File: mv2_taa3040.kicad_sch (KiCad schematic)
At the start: 13 parts, among them U1 TAA3040

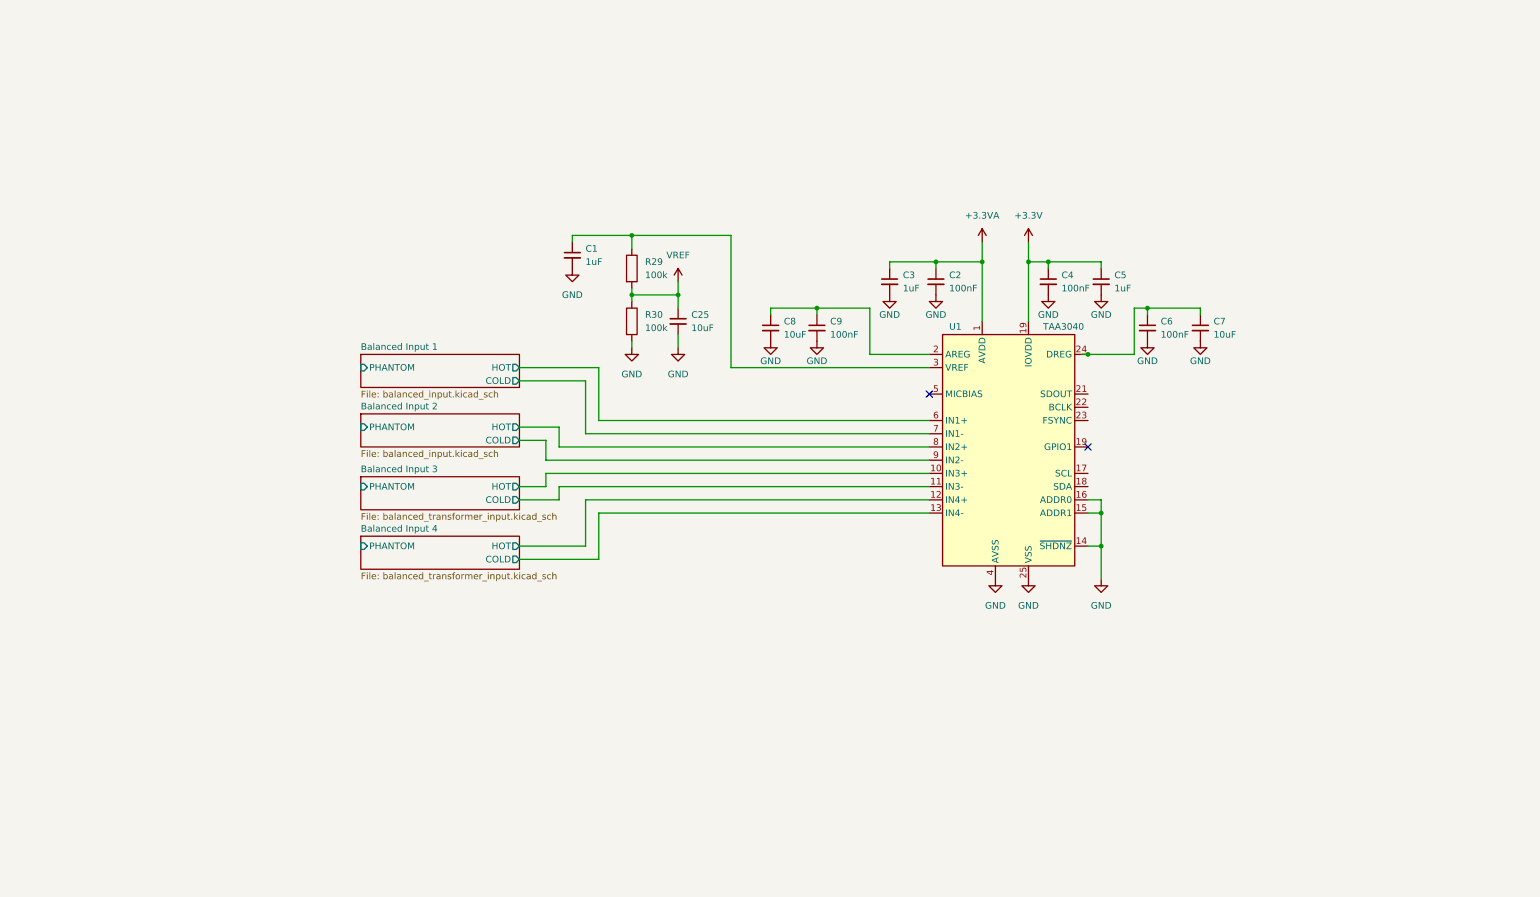
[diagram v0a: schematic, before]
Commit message: some suggested changes to the schematic:
- common pull-down mosfet for phantom power switch
- added board interconnect header
- proposed buffer for VREF
- cosmetic changes
- address selection jumpers
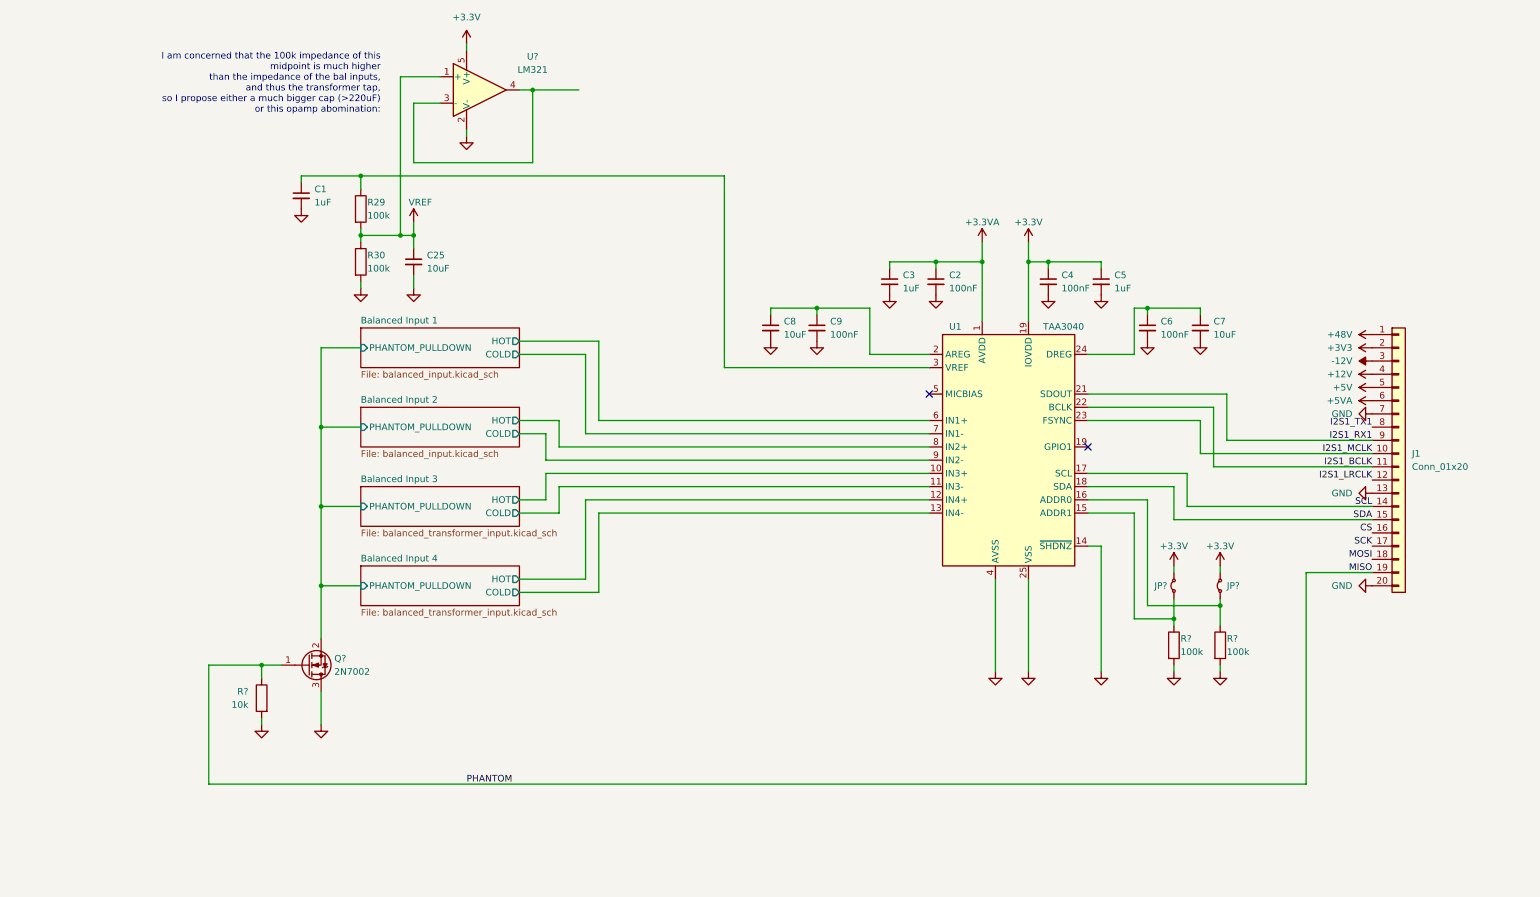
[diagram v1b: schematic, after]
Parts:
- added J1: Conn_01x20, Connector_PinHeader_2.54mm:PinHeader_1x20_P2.54mm_Vertical, symbol Connector_Generic:Conn_01x20
- added JP? (x2): Jumper_2_Small_Bridged, symbol Jumper:Jumper_2_Small_Bridged
- added Q?: 2N7002, Package_TO_SOT_SMD:SOT-23, symbol Transistor_FET:2N7002
- added R? (x2): 100k, Resistor_SMD:R_0603_1608Metric, symbol Device:R
- added R?: 10k, Resistor_SMD:R_0603_1608Metric, symbol Device:R
- added U?: LM321, Package_TO_SOT_SMD:SOT-23-5, symbol Amplifier_Operational:LM321
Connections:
- net +3.3V: now also JP?.2 (B), JP?.2 (B), U?.5 (V+)
- net GND: now also J1.13 (Pin_13), J1.20 (Pin_20), J1.7 (Pin_7), Q?.3 (D), R?.2, R?.2, R?.2, U?.2 (V-); no longer U1.15 (ADDR1), U1.16 (ADDR0)
- net VREF: now also U?.1 (+)
- net SCL: now reaches U1.17 (SCL)
- net SCL: now also J1.14 (Pin_14)
- net SDA: now reaches U1.18 (SDA)
- net SDA: now also J1.15 (Pin_15)
- net I2S1_RX1: now reaches U1.21 (SDOUT)
- net I2S1_RX1: now also J1.9 (Pin_9)
- net I2S1_BCLK: now reaches U1.22 (BCLK)
- net I2S1_BCLK: now also J1.11 (Pin_11)
- net I2S1_MCLK: now reaches U1.23 (FSYNC)
- net I2S1_MCLK: now also J1.10 (Pin_10)
- new net: U?.3 (-), U?.4
- new net: JP?.1 (A), R?.1, U1.16 (ADDR0)
- new net: JP?.1 (A), R?.1, U1.15 (ADDR1)
- new net +12V: J1.4 (Pin_4)
- new net +3V3: J1.2 (Pin_2)
- new net +48V: J1.1 (Pin_1)
- new net +5V: J1.5 (Pin_5)
- new net +5VA: J1.6 (Pin_6)
- new net -12V: J1.3 (Pin_3)
- new net Balanced Input 1/PHANTOM_PULLDOWN: Q?.2 (S)
- new net CS: J1.16 (Pin_16)
- new net I2S1_LRCLK: J1.12 (Pin_12)
- new net I2S1_TX1: J1.8 (Pin_8)
- new net MISO: J1.19 (Pin_19), Q?.1 (G), R?.1
- new net MOSI: J1.18 (Pin_18)
- new net SCK: J1.17 (Pin_17)
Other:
- sheet Balanced Input 1 ports: added PHANTOM_PULLDOWN; removed PHANTOM
- sheet Balanced Input 2 ports: added PHANTOM_PULLDOWN; removed PHANTOM
- sheet Balanced Input 3 ports: added PHANTOM_PULLDOWN; removed PHANTOM
- sheet Balanced Input 4 ports: added PHANTOM_PULLDOWN; removed PHANTOM
- note added: "I am concerned that the 100k impedance of this midpoint is much higher than the impedance of the bal inputs, and thus the transformer tap, so I propose either a much bigger cap (>220uF) or this opamp abomination:"
- moved on the sheet: C1, C25, R29, R30

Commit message: independent phantom control and removed transformer bias
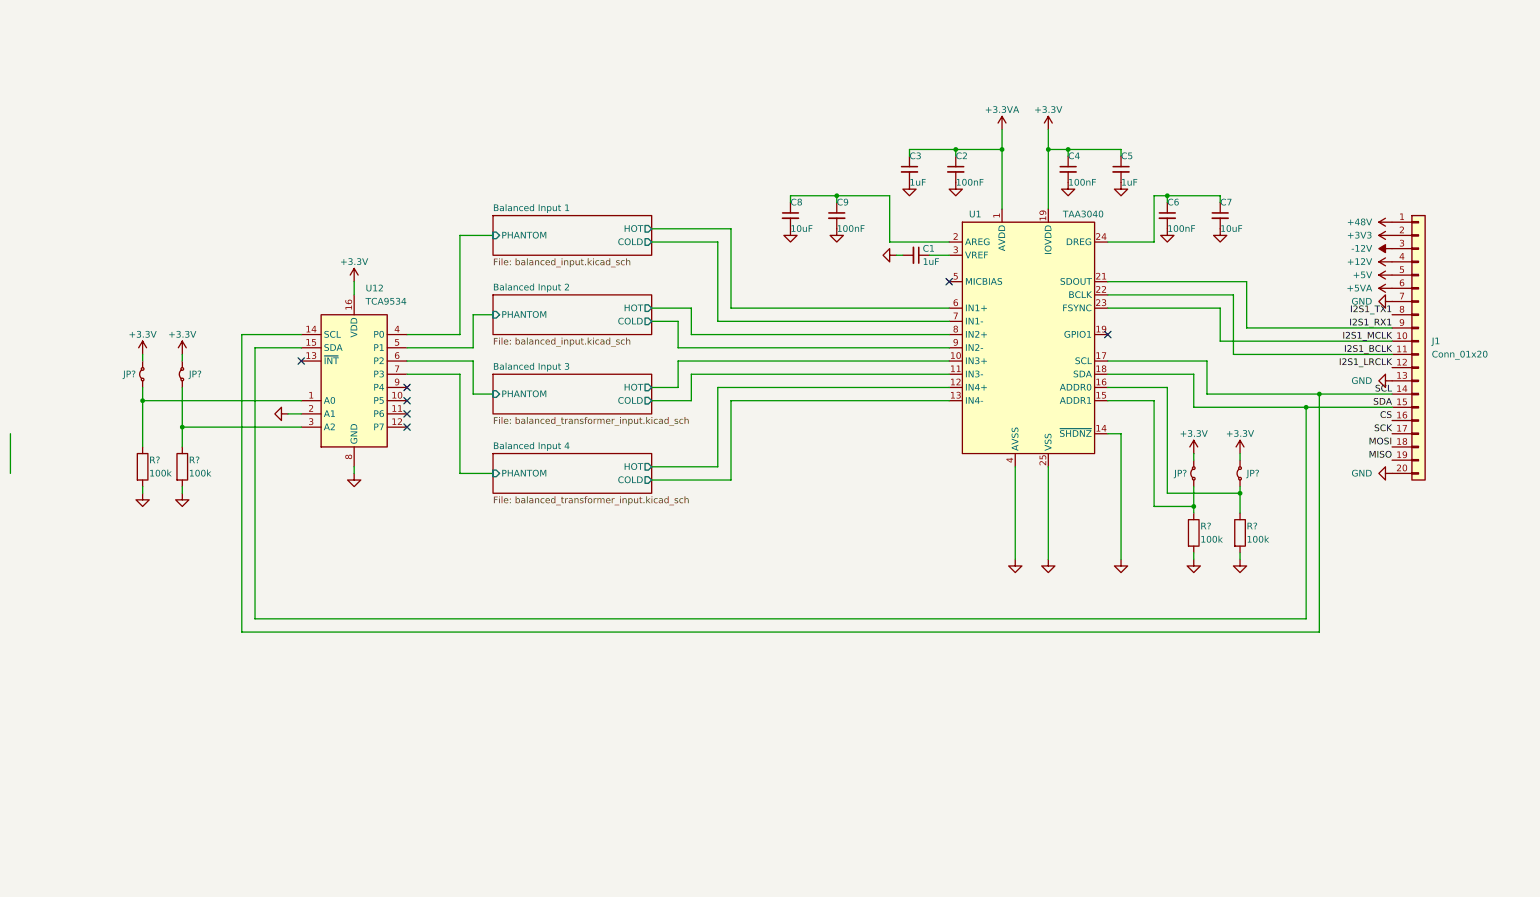
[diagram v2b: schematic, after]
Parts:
- removed C25: 10uF, Capacitor_SMD:C_0603_1608Metric, symbol Device:C_Small
- removed Q?: 2N7002, Package_TO_SOT_SMD:SOT-23, symbol Transistor_FET:2N7002
- removed R29, R30: 100k, Resistor_SMD:R_0603_1608Metric, symbol Device:R
- removed R?: 10k, Resistor_SMD:R_0603_1608Metric, symbol Device:R
- removed U?: LM321, Package_TO_SOT_SMD:SOT-23-5, symbol Amplifier_Operational:LM321
- added JP? (x2): Jumper_2_Small_Bridged, symbol Jumper:Jumper_2_Small_Bridged
- added R? (x2): 100k, Resistor_SMD:R_0603_1608Metric, symbol Device:R
- added U12: TCA9534, Package_SO:SOIC-16W_7.5x10.3mm_P1.27mm, symbol Interface_Expansion:TCA9534
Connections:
- net +3.3V: now also JP?.2 (B), JP?.2 (B), U12.16 (VDD)
- net GND: now also R?.2, R?.2, U12.2 (A1), U12.8 (GND)
- net SCL: now also U12.14 (SCL)
- net SDA: now also U12.15 (SDA)
- new net: JP?.1 (A), R?.1, U12.1 (A0)
- new net: JP?.1 (A), R?.1, U12.3 (A2)
- new net Balanced Input 1/PHANTOM: U12.4 (P0)
- new net Balanced Input 2/PHANTOM: U12.5 (P1)
- new net Balanced Input 3/PHANTOM: U12.6 (P2)
- new net Balanced Input 4/PHANTOM: U12.7 (P3)
- no-connect marks 2 -> 7
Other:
- sheet Balanced Input 1 ports: added PHANTOM; removed PHANTOM_PULLDOWN
- sheet Balanced Input 2 ports: added PHANTOM; removed PHANTOM_PULLDOWN
- sheet Balanced Input 3 ports: added PHANTOM; removed PHANTOM_PULLDOWN
- sheet Balanced Input 4 ports: added PHANTOM; removed PHANTOM_PULLDOWN
- note removed: "I am concerned that the 100k impedance of this midpoint is much higher than the impedance of the bal inputs, and thus the transformer tap, so I propose either a much bigger cap (>220uF) or this opamp abomination:"
- moved on the sheet: C1, C2, C3, C4, C5, C6, C7, C8, C9, J1, JP?, R?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

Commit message: assign some component data
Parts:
- C1: renamed from C8; MPN (none) -> C 10μF 16V 0805
- C2: renamed from C9; MPN (none) -> C 100nF 16V 0805
- C3: MPN (none) -> C 1μF 16V 0805
- C4: renamed from C1; MPN (none) -> C 1μF 16V 0805
- C5: renamed from C2; MPN (none) -> C 100nF 16V 0805
- C6: renamed from C4; MPN (none) -> C 100nF 16V 0805
- C7: renamed from C5; MPN (none) -> C 1μF 16V 0805
- C8: renamed from C6; MPN (none) -> C 100nF 16V 0805
- C9: renamed from C7; MPN (none) -> C 10μF 16V 0805
- J1: MPN (none) -> Header_1x20
- JP1, JP2, JP3, JP4: renamed from JP?; footprint (none) -> Jumper:SolderJumper-2_P1.3mm_Open_RoundedPad1.0x1.5mm
- R1, R2, R3, R4: renamed from R?; MPN (none) -> R 100kΩ 125mW 5% 0805
- U1: renamed from U12; MPN (none) -> TCA9534DWR
- U2: renamed from U1; MPN (none) -> TAA3040IRTWR

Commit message: some final touches
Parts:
- removed J1: Conn_01x20, Connector_PinHeader_2.54mm:PinHeader_1x20_P2.54mm_Vertical, symbol Connector_Generic:Conn_01x20
- R1, R2, R3, R4: value 100k -> 100kΩ
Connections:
- net I2S1_BCLK renamed Conn and power/I2S_BCLK
- net I2S1_MCLK renamed Conn and power/I2S_MCLK
- net I2S1_RX1 renamed Conn and power/I2S_RX
- net SCL renamed Conn and power/SCL
- net SDA renamed Conn and power/SDA
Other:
- added sheet Conn and power (conn_and_power.kicad_sch)

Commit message: update component assignments
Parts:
- C1, C3, C4, C7, C9: footprint Capacitor_SMD:C_0603_1608Metric -> Capacitor_SMD:C_0805_2012Metric
- C2, C5, C6, C8: MPN C 100nF 16V 0805 -> C 100nF 16V 0603
- R1, R2, R3, R4: MPN R 100kΩ 125mW 5% 0805 -> R 100kΩ 125mW 5% 0603
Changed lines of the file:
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@@
 			)
 		)
-		(property "MPN" "C 100nF 16V 0805"
+		(property "MPN" "C 100nF 16V 0603"
 			(at 219.71 54.61 0)
 			(effects
@@
 			)
 		)
-		(property "Footprint" "Capacitor_SMD:C_0603_1608Metric"
+		(property "Footprint" "Capacitor_SMD:C_0805_2012Metric"
 			(at 171.45 62.23 0)
 			(effects
@@
 			)
 		)
-		(property "MPN" "R 100kΩ 125mW 5% 0805"
+		(property "MPN" "R 100kΩ 125mW 5% 0603"
 			(at 30.48 102.87 0)
 			(effects
@@
 			)
 		)
-		(property "Footprint" "Capacitor_SMD:C_0603_1608Metric"
+		(property "Footprint" "Capacitor_SMD:C_0805_2012Metric"
 			(at 229.87 54.61 0)
 			(effects
@@
 			)
 		)
-		(property "MPN" "C 100nF 16V 0805"
+		(property "MPN" "C 100nF 16V 0603"
 			(at 179.07 45.72 0)
 			(effects
@@
 			)
 		)
-		(property "MPN" "R 100kΩ 125mW 5% 0805"
+		(property "MPN" "R 100kΩ 125mW 5% 0603"
 			(at 233.68 115.57 0)
 			(effects
@@
 			)
 		)
-		(property "MPN" "C 100nF 16V 0805"
+		(property "MPN" "C 100nF 16V 0603"
 			(at 200.66 45.72 0)
 			(effects
@@
 			)
 		)
-		(property "MPN" "C 100nF 16V 0805"
+		(property "MPN" "C 100nF 16V 0603"
 			(at 156.21 54.61 0)
 			(effects
@@
 			)
 		)
-		(property "MPN" "R 100kΩ 125mW 5% 0805"
+		(property "MPN" "R 100kΩ 125mW 5% 0603"
 			(at 22.86 102.87 0)
 			(effects
@@
 			)
 		)
-		(property "Footprint" "Capacitor_SMD:C_0603_1608Metric"
+		(property "Footprint" "Capacitor_SMD:C_0805_2012Metric"
 			(at 210.82 45.72 0)
 			(effects
@@
 			)
 		)
-		(property "Footprint" "Capacitor_SMD:C_0603_1608Metric"
+		(property "Footprint" "Capacitor_SMD:C_0805_2012Metric"
 			(at 170.18 45.72 0)
 			(effects
@@
 			)
 		)
-		(property "MPN" "R 100kΩ 125mW 5% 0805"
+		(property "MPN" "R 100kΩ 125mW 5% 0603"
 			(at 224.79 115.57 0)
 			(effects
@@
 			)
 		)
-		(property "Footprint" "Capacitor_SMD:C_0603_1608Metric"
+		(property "Footprint" "Capacitor_SMD:C_0805_2012Metric"
 			(at 147.32 54.61 0)
 			(effects

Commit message: sync pcb
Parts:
- added H1, H2, H3, H4: MountingHole_Pad, MountingHole:MountingHole_3.2mm_M3_Pad_Via, symbol Mechanical:MountingHole_Pad
- C1, C9: value 10uF -> 10μF
- C3, C4, C7: value 1uF -> 1μF
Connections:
- net GND: now also H1.1, H2.1, H3.1, H4.1
